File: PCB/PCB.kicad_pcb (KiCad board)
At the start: 2 copper layers, 33 x 25.5 mm, 17 parts, among them J1 Conn_01x06_Pin, U1 STM32G031F6P6, U2 A7106, U3 HT7333-3.3V, Y1 16MHz

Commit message: Final PCB fixes
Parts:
- removed C4: 100nF, Capacitor_SMD:C_0402_1005Metric
- removed R1: 10k, Resistor_SMD:R_0402_1005Metric
- removed TP1: SWDIO, TestPoint:TestPoint_Pad_D1.0mm
- removed TP2: SWCLK, TestPoint:TestPoint_Pad_D1.0mm
- removed U1: STM32G031F6P6, Package_SO:TSSOP-20_4.4x6.5mm_P0.65mm
- added C10: 1.5nF, Capacitor_SMD:C_0402_1005Metric, F.Cu at (154.4, 99.8)
- added C11: 100nF, Capacitor_SMD:C_0402_1005Metric, F.Cu at (154.4, 101.8)
- added C12: 100nF, Capacitor_SMD:C_0402_1005Metric, F.Cu at (154.4, 103.8)
- added C13: 100nF, Capacitor_SMD:C_0402_1005Metric, F.Cu at (154.4, 105.7)
- added C14: 100nF, Capacitor_SMD:C_0402_1005Metric, F.Cu at (154.4, 107.7)
- added C9: 100nF, Capacitor_SMD:C_0402_1005Metric, F.Cu at (151.5, 109.7)
- added TP3: SWDIO, TestPoint:TestPoint_Pad_D1.0mm, F.Cu at (163.5, 106.6)
- added TP4: SWCLK, TestPoint:TestPoint_Pad_D1.0mm, F.Cu at (163.5, 109.7)
- added U4: STM32G031F6Px, Package_SO:TSSOP-20_4.4x6.5mm_P0.65mm, F.Cu at (154.9, 94.8)
- C2, C3: value 22pF -> 18pF
- moved Y1 55.8 mm to (161.9, 93.1)
- moved U3 52.3 mm to (159.2, 108.2)
- moved C5 50.5 mm to (151.5, 105.7)
- moved C6 50.5 mm to (151.5, 107.7)
- moved C1 49.9 mm to (151.5, 99.8)
- moved C7 49.9 mm to (147.5, 109.3)
- moved C2 49.9 mm to (151.5, 101.8)
- moved C3 49.9 mm to (151.5, 103.8)
- moved L1 48.1 mm to (163.9, 99.8)
- moved ANT1 47.9 mm to (162.1, 97.1)
- moved U2 47.1 mm to (159.4, 102.0)
- moved J1 27.2 mm to (168.6, 107.8), turned to 90 degrees
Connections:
- C2 pad 1: Net-(U2-VT) -> GND
- C2 pad 2: GND -> Net-(U2-XI)
- C3 pad 1: Net-(C3-Pad1) -> Net-(U2-XO)
- C5 pad 2: Net-(U2-DVDD) -> +3.3V
- C6 pad 2: unconnected-(C6-Pad2) -> Net-(U2-RSSI)
- C7 pad 1: Net-(J1-Pin_2) -> GND
- C7 pad 2: Net-(U3-VIN) -> Net-(J1-Pin_2)
- J1 pad 3: /CH1 -> /CH4
- J1 pad 4: /CH2 -> /CH3
- J1 pad 5: /CH3 -> /CH2
- J1 pad 6: /CH4 -> /CH1
- L1 pad 1: Net-(U2-BPBG) -> Net-(U2-RFO)
- U2 pad 1: Net-(ANT1-PCB_Trace) -> Net-(U2-RSSI)
- U2 pad 10: unconnected-(U2-VDA3-Pad10) -> /VDA3
- U2 pad 13: Net-(U2-DVDD) -> +3.3V
- U2 pad 19: Net-(U2-REGI) -> +3.3V
- U2 pad 20: +3.3V -> /VDA3
- U2 pad 3: unconnected-(U2-RFI-Pad3) -> Net-(ANT1-PCB_Trace)
- U2 pad 4: unconnected-(U2-RFO-Pad4) -> Net-(U2-RFO)
- U2 pad 5: +3.3V -> /VDA3
- U2 pad 7: Net-(C3-Pad1) -> GND
- U2 pad 8: +3.3V -> Net-(U2-XI)
- U2 pad 9: unconnected-(U2-XO-Pad9) -> Net-(U2-XO)
- U3 pad 1: Net-(U3-VIN) -> Net-(J1-Pin_2)
- Y1 pad 1: GND -> Net-(U2-XI)
- Y1 pad 2: Net-(C3-Pad1) -> Net-(U2-XO)
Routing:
- net (no net): track 110.8 -> 0.00 mm, vias 11 -> 0
- net GND: track 88.0 -> 0.00 mm, vias 1 -> 0
- net Net-(U2-BPBG): track 51.2 -> 0.00 mm, vias 4 -> 0
- net Net-(U3-VIN): track 30.4 -> 0.00 mm
- net Net-(C1-Pad1): track 19.7 -> 0.00 mm, vias 2 -> 0
- net Net-(U1-VDD): track 15.6 -> 0.00 mm, vias 2 -> 0
- net Net-(J1-Pin_2): track 14.6 -> 0.00 mm
- net /SCS: track 14.2 -> 0.00 mm, vias 2 -> 0
- net /SCK: track 12.4 -> 0.00 mm, vias 2 -> 0
- net /SDIO: track 11.9 -> 0.00 mm, vias 2 -> 0
- net Net-(U1-NRST): track 9.05 -> 0.00 mm
- net /GIO1: track 8.34 -> 0.00 mm, vias 2 -> 0
- net Net-(ANT1-FEED): track 7.92 -> 0.00 mm
- net Net-(ANT1-PCB_Trace): track 7.91 -> 0.00 mm
- net Net-(U1-PA13): track 7.89 -> 0.00 mm
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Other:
- board size 33 x 25.5 mm -> 16.5 x 18 mm

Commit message: Antenna fixes
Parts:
- added C8: 1µF, Capacitor_SMD:C_0402_1005Metric, F.Cu at (152.2, 110.7)
- added R1: 10k, Resistor_SMD:R_0402_1005Metric, F.Cu at (152.2, 108.7)
- moved L1 16.9 mm to (149.5, 108.6)
- moved Y1 16.6 mm to (150.6, 105.3)
- moved C7 15.1 mm to (162.4, 106.7)
- moved TP3 13.9 mm to (164.4, 92.8)
- moved TP4 13.9 mm to (164.4, 95.8)
- moved ANT1 11.6 mm to (156.6, 107.3)
- moved C2 7.89 mm to (149.4, 94.2)
- moved C3 7.89 mm to (149.4, 96.2)
- moved C5 7.89 mm to (149.4, 98.1)
- moved C6 7.89 mm to (149.4, 100.1)
- moved C9 7.89 mm to (149.4, 102.1)
- moved C11 7.89 mm to (152.3, 94.2)
- moved C12 7.89 mm to (152.3, 96.2)
- moved C13 7.89 mm to (152.3, 98.1)
- moved C14 7.89 mm to (152.3, 100.1)
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
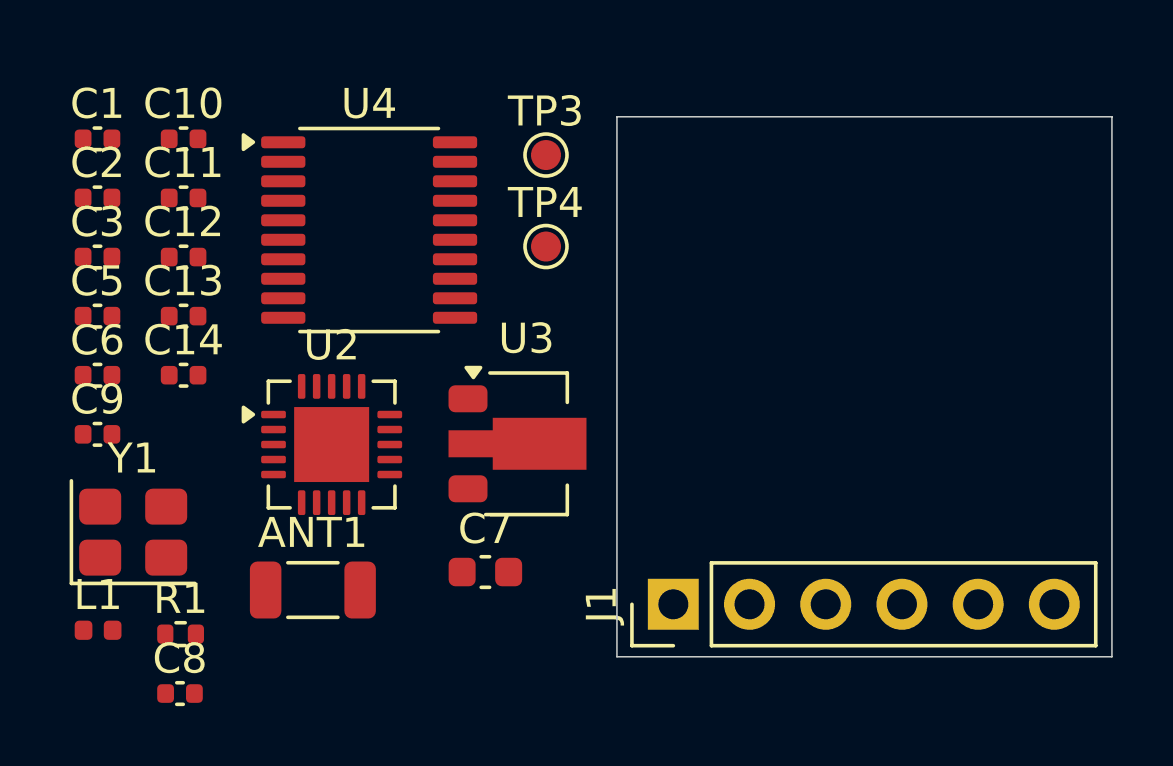
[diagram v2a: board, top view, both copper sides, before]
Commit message: Add battery voltage reader
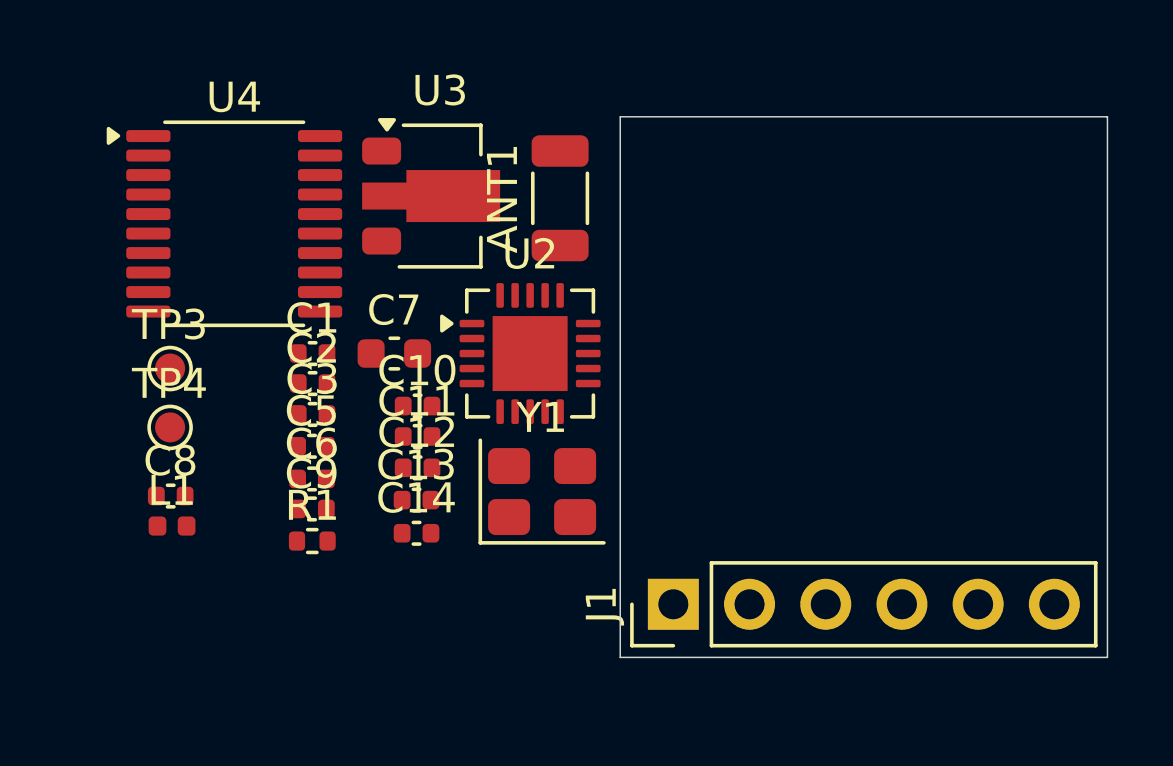
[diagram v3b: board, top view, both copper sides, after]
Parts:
- moved ANT1 15.4 mm to (164.9, 94.2), turned to 90 degrees
- moved TP3 14.4 mm to (151.9, 99.9)
- moved TP4 13.9 mm to (151.9, 101.9)
- moved Y1 13.7 mm to (164.3, 104.0)
- moved C10 11.8 mm to (160.1, 101.1)
- moved C11 11.1 mm to (160.1, 102.2)
- moved C12 10.5 mm to (160.1, 103.2)
- moved C1 10.1 mm to (156.6, 99.4)
- moved C13 9.89 mm to (160.1, 104.3)
- moved C2 9.47 mm to (156.6, 100.4)
- moved C14 9.38 mm to (160.1, 105.4)
- moved C3 8.88 mm to (156.6, 101.4)
- moved U3 8.75 mm to (160.9, 94.1)
- moved C5 8.36 mm to (156.6, 102.5)
- moved C6 7.94 mm to (156.6, 103.6)
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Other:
- board size 16.5 x 18 mm -> 16.2 x 18 mm
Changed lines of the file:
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@@
 	(footprint "Capacitor_SMD:C_0402_1005Metric"
 		(layer "F.Cu")
-		(at 149.435 92.235)
+		(at 156.605 99.392)
 		(descr "Capacitor SMD 0402 (1005 Metric), square (rectangular) end terminal, IPC-7351 nominal, (Body size source: IPC-SM-782 page 76, https://www.pcb-3d.com/wordpress/wp-content/uploads/ipc-sm-782a_amendment_1_and_2.pdf)")
 		(tags "capacitor")
@@
 	(footprint "Capacitor_SMD:C_0402_1005Metric"
 		(layer "F.Cu")
-		(at 152.305 96.175)
+		(at 160.105 103.202)
 		(descr "Capacitor SMD 0402 (1005 Metric), square (rectangular) end terminal, IPC-7351 nominal, (Body size source: IPC-SM-782 page 76, https://www.pcb-3d.com/wordpress/wp-content/uploads/ipc-sm-782a_amendment_1_and_2.pdf)")
 		(tags "capacitor")
@@
 	(footprint "Crystal:Crystal_SMD_3225-4Pin_3.2x2.5mm"
 		(layer "F.Cu")
-		(at 150.625 105.345)
+		(at 164.255 103.992)
 		(descr "SMD3225/4, Crystal, 3.2x2.5mm package, SMD, http://www.txccrystal.com/images/pdf/7m-accuracy.pdf")
 		(property "Reference" "Y1"
@@
 	(footprint "Capacitor_SMD:C_0402_1005Metric"
 		(layer "F.Cu")
-		(at 152.305 100.115)
+		(at 160.07 105.382)
 		(descr "Capacitor SMD 0402 (1005 Metric), square (rectangular) end terminal, IPC-7351 nominal, (Body size source: IPC-SM-782 page 76, https://www.pcb-3d.com/wordpress/wp-content/uploads/ipc-sm-782a_amendment_1_and_2.pdf)")
 		(tags "capacitor")
@@
 	(footprint "Inductor_SMD:L_1206_3216Metric"
 		(layer "F.Cu")
-		(at 156.615 107.275)
+		(at 164.855 94.217 90)
 		(descr "Inductor SMD 1206 (3216 Metric), square (rectangular) end terminal, IPC-7351 nominal, (Body size source: IPC-SM-782 page 80, https://www.pcb-3d.com/wordpress/wp-content/uploads/ipc-sm-782a_amendment_1_and_2.pdf)")
 		(tags "inductor")
 		(property "Reference" "ANT1"
-			(at 0 -1.9 0)
+			(at 0 -1.9 90)
 			(layer "F.SilkS")
 			(effects
@@
 		)
 		(property "Value" "RFANT3216120A5T"
-			(at 0 1.9 0)
+			(at 0 1.9 90)
 			(layer "F.Fab")
 			(effects
@@
 		)
 		(property "Datasheet" "~"
-			(at 0 0 0)
+			(at 0 0 90)
 			(layer "F.Fab")
 			(hide yes)
@@
 		)
 		(property "Description" ""
-			(at 0 0 0)
+			(at 0 0 90)
 			(layer "F.Fab")
 			(hide yes)
@@
 		)
 		(property "KiLib_Generator" "SMD_2terminal_chip_molded"
-			(at 0 0 0)
+			(at 0 0 90)
 			(layer "F.SilkS")
 			(hide yes)
@@
 		)
 		(property "LCSC" "C127629"
-			(at 0 0 0)
+			(at 0 0 90)
 			(unlocked yes)
 			(layer "F.Fab")
@@
 		)
 		(fp_text user "${REFERENCE}"
-			(at 0 0 0)
+			(at 0 0 90)
 			(layer "F.Fab")
 			(effects
@@
 		)
 		(pad "1" smd roundrect
-			(at -1.575 0)
+			(at -1.575 0 90)
 			(size 1.05 1.9)
 			(layers "F.Cu" "F.Mask" "F.Paste")
@@
 		)
 		(pad "2" smd roundrect
-			(at 1.575 0)
+			(at 1.575 0 90)
 			(size 1.05 1.9)
 			(layers "F.Cu" "F.Mask" "F.Paste")
@@
 	(footprint "Capacitor_SMD:C_0402_1005Metric"
 		(layer "F.Cu")
-		(at 152.305 92.235)
+		(at 160.105 101.142)
 		(descr "Capacitor SMD 0402 (1005 Metric), square (rectangular) end terminal, IPC-7351 nominal, (Body size source: IPC-SM-782 page 76, https://www.pcb-3d.com/wordpress/wp-content/uploads/ipc-sm-782a_amendment_1_and_2.pdf)")
 		(tags "capacitor")
@@
 	(footprint "Capacitor_SMD:C_0402_1005Metric"
 		(layer "F.Cu")
-		(at 152.185 110.725)
+		(at 151.875 104.142)
 		(descr "Capacitor SMD 0402 (1005 Metric), square (rectangular) end terminal, IPC-7351 nominal, (Body size source: IPC-SM-782 page 76, https://www.pcb-3d.com/wordpress/wp-content/uploads/ipc-sm-782a_amendment_1_and_2.pdf)")
 		(tags "capacitor")
@@
 	(footprint "Capacitor_SMD:C_0402_1005Metric"
 		(layer "F.Cu")
-		(at 149.435 100.115)
+		(at 156.585 103.572)
 		(descr "Capacitor SMD 0402 (1005 Metric), square (rectangular) end terminal, IPC-7351 nominal, (Body size source: IPC-SM-782 page 76, https://www.pcb-3d.com/wordpress/wp-content/uploads/ipc-sm-782a_amendment_1_and_2.pdf)")
 		(tags "capacitor")
@@
 	(footprint "Package_TO_SOT_SMD:SOT-89-3"
 		(layer "F.Cu")
-		(at 163.735 102.4)
+		(at 160.855 94.142)
 		(descr "SOT-89-3, http://ww1.microchip.com/downloads/en/DeviceDoc/3L_SOT-89_MB_C04-029C.pdf")
 		(tags "SOT-89-3")
@@
 	(footprint "Capacitor_SMD:C_0402_1005Metric"
 		(layer "F.Cu")
-		(at 149.435 94.205)
+		(at 156.605 100.392)
 		(descr "Capacitor SMD 0402 (1005 Metric), square (rectangular) end terminal, IPC-7351 nominal, (Body size source: IPC-SM-782 page 76, https://www.pcb-3d.com/wordpress/wp-content/uploads/ipc-sm-782a_amendment_1_and_2.pdf)")
 		(tags "capacitor")
@@
 	(footprint "Package_DFN_QFN:QFN-20-1EP_4x4mm_P0.5mm_EP2.5x2.5mm"
 		(layer "F.Cu")
-		(at 157.24 102.425)
+		(at 163.855 99.392)
 		(descr "QFN, 20 Pin (http://ww1.microchip.com/downloads/en/PackagingSpec/00000049BQ.pdf#page=274)")
 		(tags "QFN NoLead")
@@
 	(footprint "Capacitor_SMD:C_0402_1005Metric"
 		(layer "F.Cu")
-		(at 152.305 94.205)
+		(at 160.105 102.157)
 		(descr "Capacitor SMD 0402 (1005 Metric), square (rectangular) end terminal, IPC-7351 nominal, (Body size source: IPC-SM-782 page 76, https://www.pcb-3d.com/wordpress/wp-content/uploads/ipc-sm-782a_amendment_1_and_2.pdf)")
 		(tags "capacitor")
@@
 	(footprint "Package_SO:TSSOP-20_4.4x6.5mm_P0.65mm"
 		(layer "F.Cu")
-		(at 158.49 95.275)
+		(at 153.9925 95.067)
 		(descr "TSSOP, 20 Pin (JEDEC MO-153 Var AC https://www.jedec.org/document_search?search_api_views_fulltext=MO-153)")
 		(tags "TSSOP SO")
@@
 	(footprint "TestPoint:TestPoint_Pad_D1.0mm"
 		(layer "F.Cu")
-		(at 164.385 92.775)
+		(at 151.855 99.892)
 		(descr "SMD pad as test Point, diameter 1.0mm")
 		(tags "test point SMD pad")
@@
 	(footprint "Capacitor_SMD:C_0402_1005Metric"
 		(layer "F.Cu")
-		(at 152.305 98.145)
+		(at 160.07 104.277)
 		(descr "Capacitor SMD 0402 (1005 Metric), square (rectangular) end terminal, IPC-7351 nominal, (Body size source: IPC-SM-782 page 76, https://www.pcb-3d.com/wordpress/wp-content/uploads/ipc-sm-782a_amendment_1_and_2.pdf)")
 		(tags "capacitor")
@@
 	(footprint "Capacitor_SMD:C_0402_1005Metric"
 		(layer "F.Cu")
-		(at 149.435 98.145)
+		(at 156.585 102.482)
 		(descr "Capacitor SMD 0402 (1005 Metric), square (rectangular) end terminal, IPC-7351 nominal, (Body size source: IPC-SM-782 page 76, https://www.pcb-3d.com/wordpress/wp-content/uploads/ipc-sm-782a_amendment_1_and_2.pdf)")
 		(tags "capacitor")
@@
 	(footprint "TestPoint:TestPoint_Pad_D1.0mm"
 		(layer "F.Cu")
-		(at 164.385 95.825)
+		(at 151.855 101.854)
 		(descr "SMD pad as test Point, diameter 1.0mm")
 		(tags "test point SMD pad")
@@
 	(footprint "Capacitor_SMD:C_0402_1005Metric"
 		(layer "F.Cu")
-		(at 149.435 96.175)
+		(at 156.605 101.422)
 		(descr "Capacitor SMD 0402 (1005 Metric), square (rectangular) end terminal, IPC-7351 nominal, (Body size source: IPC-SM-782 page 76, https://www.pcb-3d.com/wordpress/wp-content/uploads/ipc-sm-782a_amendment_1_and_2.pdf)")
 		(tags "capacitor")
@@
 	(footprint "Capacitor_SMD:C_0603_1608Metric"
 		(layer "F.Cu")
-		(at 162.365 106.675)
+		(at 159.33 99.392)
 		(descr "Capacitor SMD 0603 (1608 Metric), square (rectangular) end terminal, IPC-7351 nominal, (Body size source: IPC-SM-782 page 76, https://www.pcb-3d.com/wordpress/wp-content/uploads/ipc-sm-782a_amendment_1_and_2.pdf)")
 		(tags "capacitor")
@@
 		(embedded_fonts no)
 		(model "${KICAD10_3DMODEL_DIR}/Connector_PinHeader_2.54mm.3dshapes/PinHeader_1x06_P2.54mm_Vertical.step"
+			(opacity 0.0000)
 			(offset
 				(xyz 0 0 0)
@@
 	(footprint "Resistor_SMD:R_0402_1005Metric"
 		(layer "F.Cu")
-		(at 152.205 108.745)
+		(at 156.595 105.642)
 		(descr "Resistor SMD 0402 (1005 Metric), square (rectangular) end terminal, IPC-7351 nominal, (Body size source: IPC-SM-782 page 72, https://www.pcb-3d.com/wordpress/wp-content/uploads/ipc-sm-782a_amendment_1_and_2.pdf)")
 		(tags "resistor")
@@
 	(footprint "Inductor_SMD:L_0402_1005Metric"
 		(layer "F.Cu")
-		(at 149.455 108.615)
+		(at 151.92 105.142)
 		(descr "Inductor SMD 0402 (1005 Metric), square (rectangular) end terminal, IPC-7351 nominal, (Body size source: http://www.tortai-tech.com/upload/download/2011102023233369053.pdf)")
 		(tags "inductor")
@@
 	(footprint "Capacitor_SMD:C_0402_1005Metric"
 		(layer "F.Cu")
-		(at 149.435 102.085)
+		(at 156.585 104.572)
 		(descr "Capacitor SMD 0402 (1005 Metric), square (rectangular) end terminal, IPC-7351 nominal, (Body size source: IPC-SM-782 page 76, https://www.pcb-3d.com/wordpress/wp-content/uploads/ipc-sm-782a_amendment_1_and_2.pdf)")
 		(tags "capacitor")
@@
 	)
 	(gr_rect
-		(start 166.75 91.5)
-		(end 183.25 109.5)
+		(start 166.86 91.5)
+		(end 183.1 109.52)
 		(stroke
 			(width 0.05)
